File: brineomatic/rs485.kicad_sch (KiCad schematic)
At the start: 13 parts, among them J23 3.5mm, J24 3.5mm, U10 MAX3485

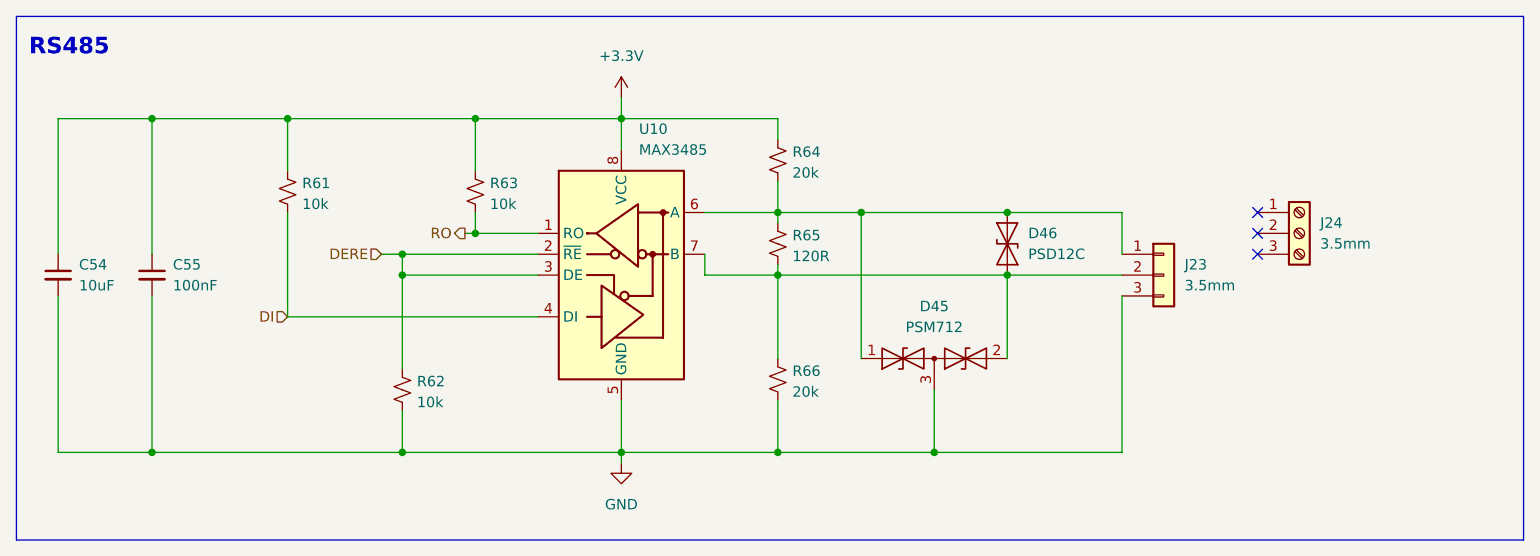
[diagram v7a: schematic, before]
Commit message: voltage divider on EN pin to turn on at 10.2v (EN = 2v) -> connect to VIN not 24v
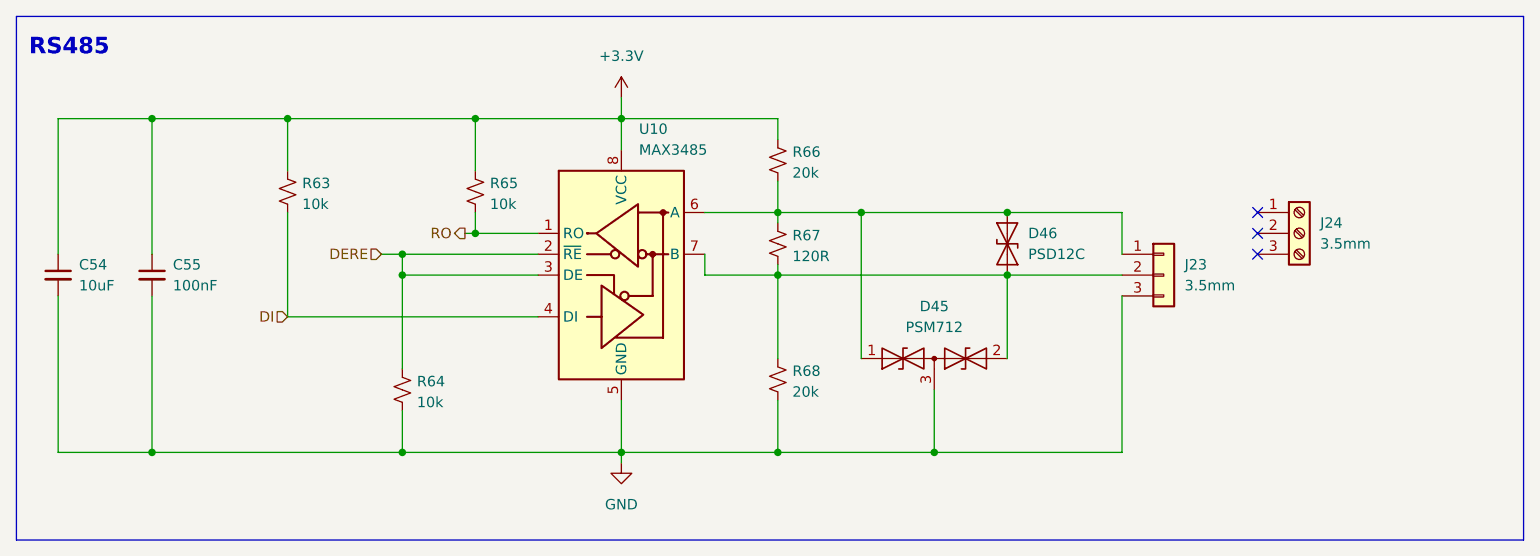
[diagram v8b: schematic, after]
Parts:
- renumbered R61 to R63, R62 to R64, R63 to R65, R64 to R66, R65 to R67, R66 to R68
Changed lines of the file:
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@@
 		(dnp no)
 		(fields_autoplaced yes)
-		(property "Reference" "#PWR072"
+		(property "Reference" "#PWR071"
 			(at 140.97 130.81 0)
 			(effects
@@
 			(project "brineomatic"
 				(path "/96477ae2-ef08-48f3-8dd4-fe4478541f68/ecabf60a-7f79-4ba0-9fc6-a1e702c2d5f0"
-					(reference "#PWR072")
+					(reference "#PWR071")
 					(unit 1)
 				)
@@
 		(on_board yes)
 		(dnp no)
-		(property "Reference" "R66"
+		(property "Reference" "R68"
 			(at 161.798 113.284 0)
 			(effects
@@
 			(project "brineomatic"
 				(path "/96477ae2-ef08-48f3-8dd4-fe4478541f68/ecabf60a-7f79-4ba0-9fc6-a1e702c2d5f0"
-					(reference "R66")
+					(reference "R68")
 					(unit 1)
 				)
@@
 		(on_board yes)
 		(dnp no)
-		(property "Reference" "R61"
+		(property "Reference" "R63"
 			(at 102.108 90.424 0)
 			(effects
@@
 			(project "brineomatic"
 				(path "/96477ae2-ef08-48f3-8dd4-fe4478541f68/ecabf60a-7f79-4ba0-9fc6-a1e702c2d5f0"
-					(reference "R61")
+					(reference "R63")
 					(unit 1)
 				)
@@
 		(on_board yes)
 		(dnp no)
-		(property "Reference" "R63"
+		(property "Reference" "R65"
 			(at 124.968 90.424 0)
 			(effects
@@
 			(project "brineomatic"
 				(path "/96477ae2-ef08-48f3-8dd4-fe4478541f68/ecabf60a-7f79-4ba0-9fc6-a1e702c2d5f0"
-					(reference "R63")
+					(reference "R65")
 					(unit 1)
 				)
@@
 		(on_board yes)
 		(dnp no)
-		(property "Reference" "R65"
+		(property "Reference" "R67"
 			(at 161.798 96.774 0)
 			(effects
@@
 			(project "brineomatic"
 				(path "/96477ae2-ef08-48f3-8dd4-fe4478541f68/ecabf60a-7f79-4ba0-9fc6-a1e702c2d5f0"
-					(reference "R65")
+					(reference "R67")
 					(unit 1)
 				)
@@
 		(dnp no)
 		(fields_autoplaced yes)
-		(property "Reference" "#PWR071"
+		(property "Reference" "#PWR070"
 			(at 140.97 83.82 0)
 			(effects
@@
 			(project ""
 				(path "/96477ae2-ef08-48f3-8dd4-fe4478541f68/ecabf60a-7f79-4ba0-9fc6-a1e702c2d5f0"
-					(reference "#PWR071")
+					(reference "#PWR070")
 					(unit 1)
 				)
@@
 		(on_board yes)
 		(dnp no)
-		(property "Reference" "R62"
+		(property "Reference" "R64"
 			(at 116.078 114.554 0)
 			(effects
@@
 			(project "brineomatic"
 				(path "/96477ae2-ef08-48f3-8dd4-fe4478541f68/ecabf60a-7f79-4ba0-9fc6-a1e702c2d5f0"
-					(reference "R62")
+					(reference "R64")
 					(unit 1)
 				)
@@
 		(on_board yes)
 		(dnp no)
-		(property "Reference" "R64"
+		(property "Reference" "R66"
 			(at 161.798 86.614 0)
 			(effects
@@
 			(project "brineomatic"
 				(path "/96477ae2-ef08-48f3-8dd4-fe4478541f68/ecabf60a-7f79-4ba0-9fc6-a1e702c2d5f0"
-					(reference "R64")
-					(unit 1)
-				)
+					(reference "R66")
+					(unit 1)
+				)
